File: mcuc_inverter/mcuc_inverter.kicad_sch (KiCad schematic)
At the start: 0 parts

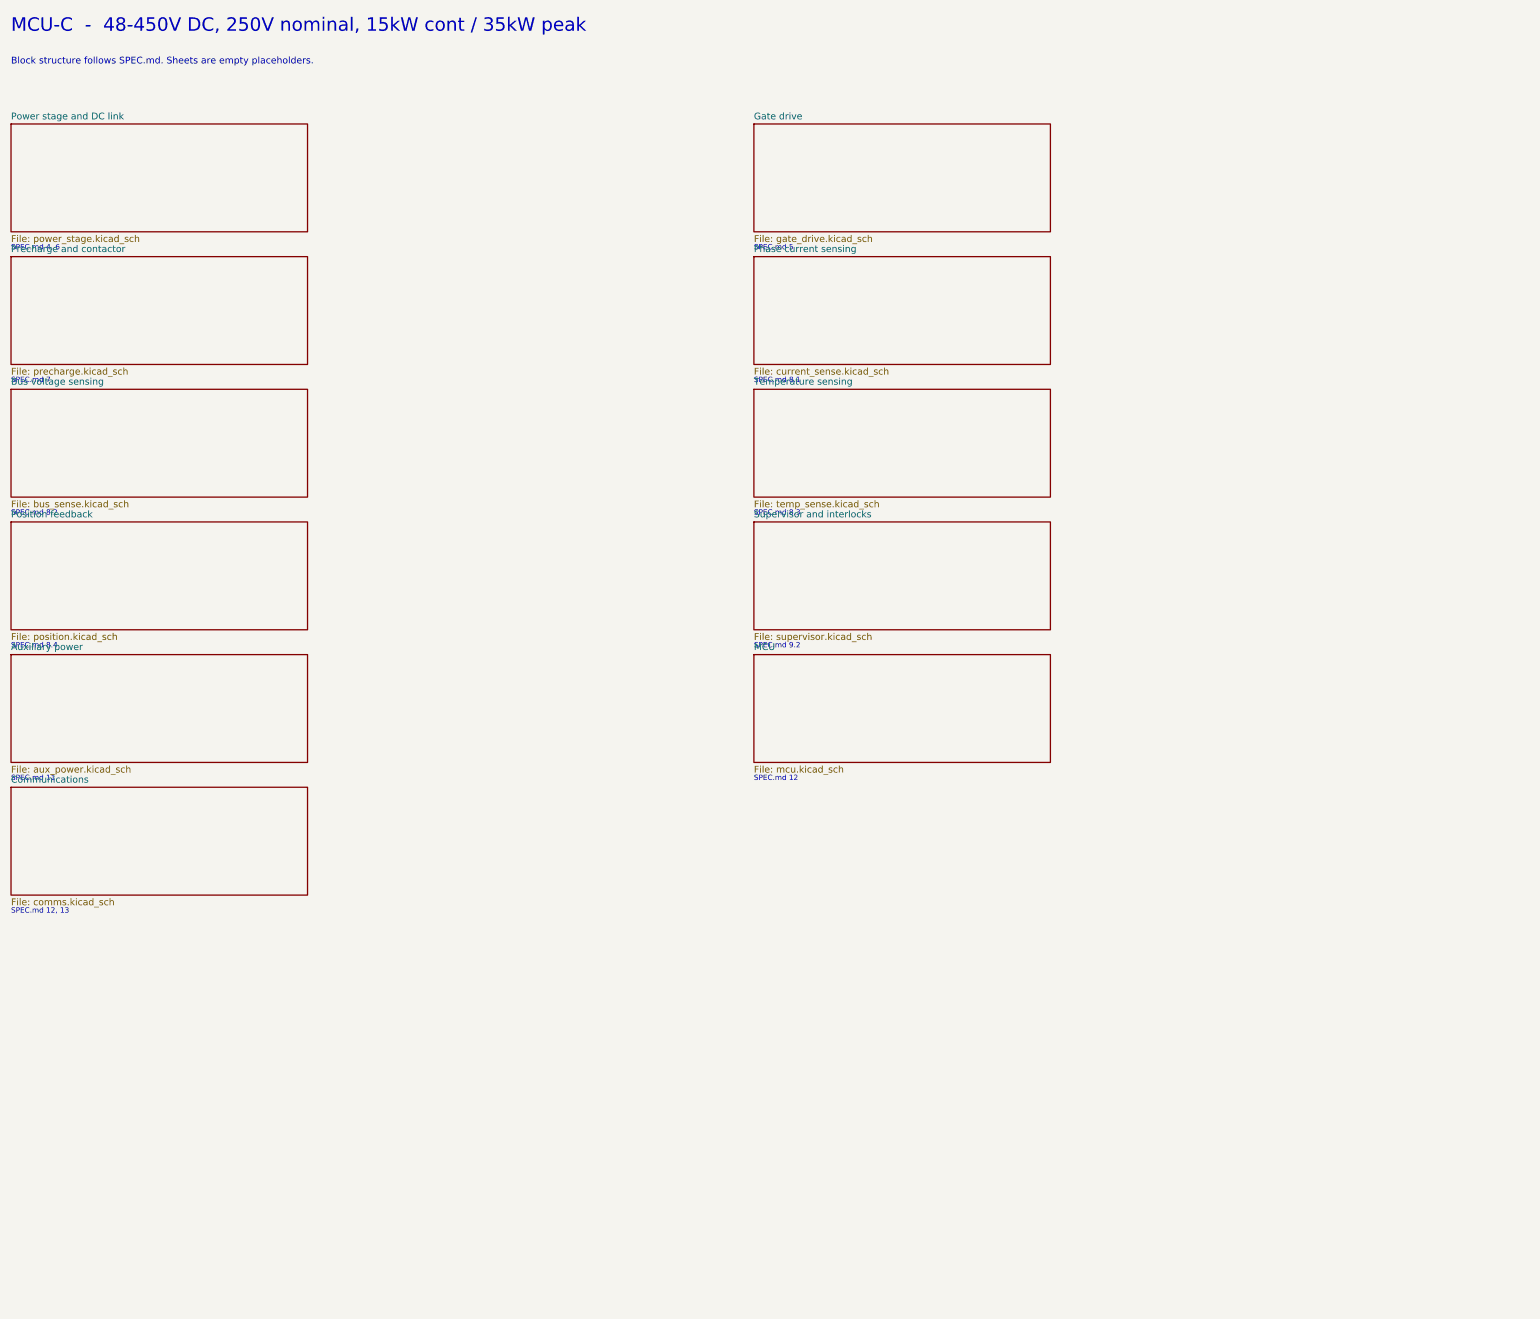
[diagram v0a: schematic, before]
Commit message: Design the supervisor interlock block
Adds docs/supervisor.md: the full logic design for the firmware-independent
hardware interlocks required by SPEC.md §9.2 -- overcurrent detect and latch,
fault aggregation, PWM overlap elimination and dead time. Includes the
24-signal interface, gate budget, and a failure-mode review done on the
assumption that firmware is hostile.

Two selections differ from the original PALTA board, both deliberate:

- Comparators run from +5 V, not 3.3 V. The LM2903's input common-mode
  ceiling is VCC-1.5V, so on 3.3 V it is 1.8 V -- below the 3.05 V positive
  trip point. The positive-overcurrent channel would never have asserted.
  Open-drain outputs still pull up to 3.3 V, so no level shifting is needed.
- 74HC replaces 74ACT. The dead-time RC assumes a CMOS threshold at
  0.5*VCC; 74ACT's TTL thresholds make the delay supply- and part-dependent.
  Predictable dead time beats ~10 ns of propagation delay here.

Adds tools/gen_skeleton.py, which generates the KiCad skeleton and records
the block interfaces, and ERC severities in mcuc_inverter.kicad_pro:
hier_label_mismatch stays an error, label_dangling and pin_not_connected
become warnings during build-out.

The interface is not emitted into the schematic yet (EMIT_INTERFACE=False).
Emitting it into empty sheets produces 96 legitimate dangling-label
violations, and copperhead check fails on warnings as well as errors, which
would leave the verification gate permanently red -- the same failure mode
that let the earlier generated documents through unchecked. The interface
lands in the same change as the components. Rationale in supervisor.md §9.

Verified: kicad-cli sch erc reports 0 violations and copperhead check is
green. With the interface temporarily emitted, ERC reported no
hier_label_mismatch, confirming all 24 names and directions agree across
every sheet boundary.

Co-Authored-By: Claude Opus 5 <noreply@anthropic.com>
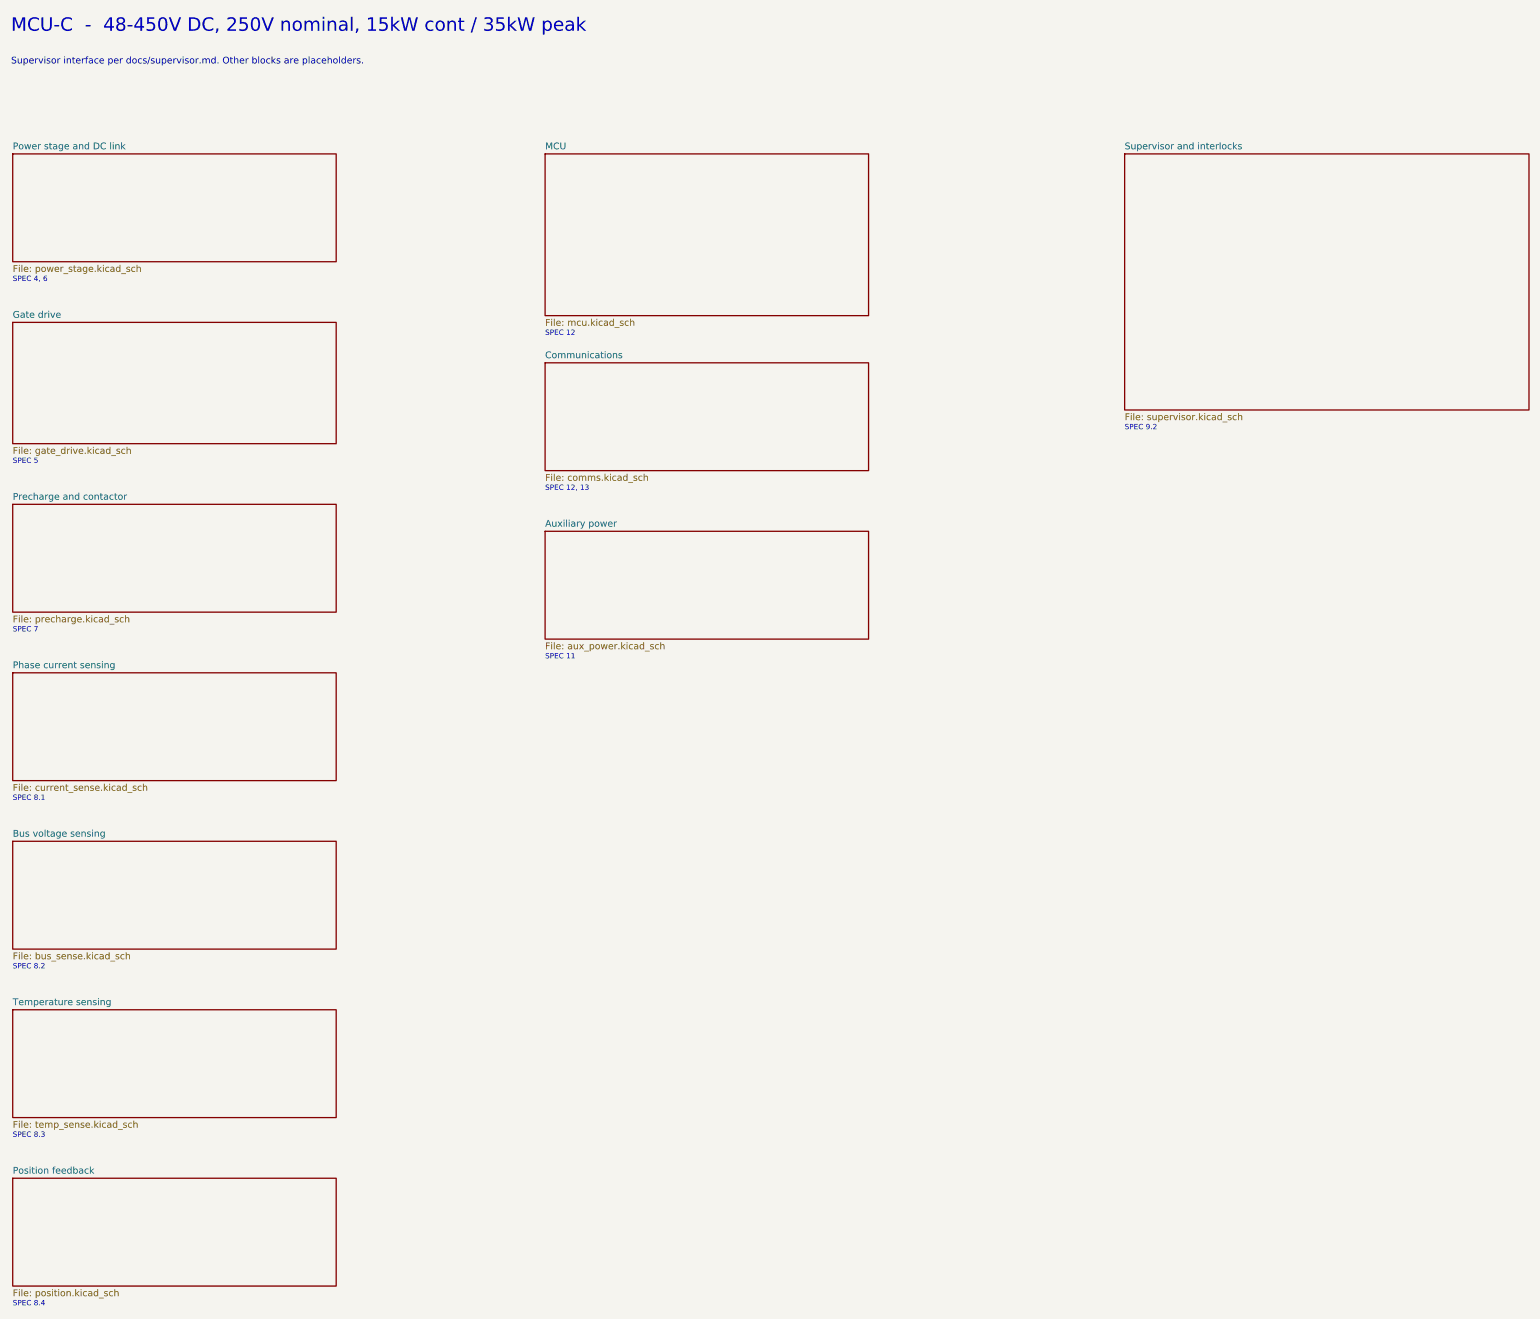
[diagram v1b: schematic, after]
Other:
- note added: "SPEC 11"
- note added: "SPEC 12"
- note added: "SPEC 12, 13"
- note added: "SPEC 4, 6"
- note added: "SPEC 5"
- note added: "SPEC 7"
- note added: "SPEC 8.1"
- note added: "SPEC 8.2"
- note added: "SPEC 8.3"
- note added: "SPEC 8.4"
- note added: "SPEC 9.2"
- note added: "Supervisor interface per docs/supervisor.md. Other blocks are placeholders."
- note removed: "Block structure follows SPEC.md. Sheets are empty placeholders."
- note removed: "SPEC.md 11"
- note removed: "SPEC.md 12"
- note removed: "SPEC.md 12, 13"
- note removed: "SPEC.md 4, 6"
- note removed: "SPEC.md 5"
- note removed: "SPEC.md 7"
- note removed: "SPEC.md 8.1"
- note removed: "SPEC.md 8.2"
- note removed: "SPEC.md 8.3"
- note removed: "SPEC.md 8.4"
- note removed: "SPEC.md 9.2"

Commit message: Place the supervisor overcurrent comparator front end
Implements docs/supervisor.md section 3 in the schematic: 13 components
across the threshold divider, six LM2903 comparator channels and the
wired-OR trip node.

A single three-resistor string (1k / 11k / 1k off +3V3) generates both
thresholds -- 3.046 V and 0.254 V, i.e. +/-280 A -- which keeps them
ratiometric with the rail the current sense is referenced to, so divider
tolerance and rail drift track out of the trip point.

Channel polarity: the positive trip puts V_TH_POS on IN+ and ISENSE on
IN-, the negative trip the other way round, so both pull the open-drain
output low on an overcurrent of either sign. All six outputs wire-OR onto
OC_TRIP_N with one 4.7k pull-up to +3V3 and a 100 pF filter.

Verified by netlist export rather than assumption:
  OC_TRIP_N  8 nodes  six comparator outputs + pull-up + filter
  V_TH_POS   6 nodes  divider tap, decoupling, three positive-channel IN+
  V_TH_NEG   6 nodes  divider tap, decoupling, three negative-channel IN-
  ISENSE_x   2 nodes  Ux.2 and Ux.5, the intended cross-pairing
  +5V        6 nodes  three LM2903 V+ and three decoupling caps
  GND       10 nodes
ERC reports 0 errors.

gen_skeleton.py now emits interface signals selectively via EMIT_SIGNALS
instead of all-or-nothing, so warnings stay proportional to what is built.
Six warnings remain -- 3 label_dangling and 3 pin_not_driven -- all saying
that current_sense does not exist yet so nothing drives ISENSE. Left in
place deliberately; they clear when that block is populated.

pin_not_driven joins the WIP warning severities. hier_label_mismatch stays
an error, since a boundary mismatch is a real defect at any build state.

Note that copperhead check fails on warnings as well as errors, so it reads
red while any block is unbuilt. kicad-cli sch erc --severity-error is the
meaningful gate during build-out and currently reports 0.

Co-Authored-By: Claude Opus 5 <noreply@anthropic.com>
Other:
- sheet Phase current sensing ports: added ISENSE_A, ISENSE_B, ISENSE_C; removed none
- sheet Supervisor and interlocks ports: added ISENSE_A, ISENSE_B, ISENSE_C; removed none
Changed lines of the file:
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@@
 		(instances
 			(project "mcuc_inverter"
-				(path "/bf2b1e33-8fc4-447a-8dc6-49e53bf48170"
+				(path "/c2a3c707-c5cb-4b38-83d3-7f8307d61589"
 					(page "2")
 				)
@@
 		(instances
 			(project "mcuc_inverter"
-				(path "/bf2b1e33-8fc4-447a-8dc6-49e53bf48170"
+				(path "/c2a3c707-c5cb-4b38-83d3-7f8307d61589"
 					(page "3")
 				)
@@
 		(instances
 			(project "mcuc_inverter"
-				(path "/bf2b1e33-8fc4-447a-8dc6-49e53bf48170"
+				(path "/c2a3c707-c5cb-4b38-83d3-7f8307d61589"
 					(page "4")
 				)
@@
 			)
 		)
-		(instances
-			(project "mcuc_inverter"
-				(path "/bf2b1e33-8fc4-447a-8dc6-49e53bf48170"
+		(pin "ISENSE_A" output
+			(at 81.28 140.97 0)
+			(effects
+				(font
+					(size 1.27 1.27)
+				)
+				(justify left)
+			)
+		)
+		(pin "ISENSE_B" output
+			(at 81.28 143.51000000000002 0)
+			(effects
+				(font
+					(size 1.27 1.27)
+				)
+				(justify left)
+			)
+		)
+		(pin "ISENSE_C" output
+			(at 81.28 146.05 0)
+			(effects
+				(font
+					(size 1.27 1.27)
+				)
+				(justify left)
+			)
+		)
+		(instances
+			(project "mcuc_inverter"
+				(path "/c2a3c707-c5cb-4b38-83d3-7f8307d61589"
 					(page "5")
 				)
@@
 		(instances
 			(project "mcuc_inverter"
-				(path "/bf2b1e33-8fc4-447a-8dc6-49e53bf48170"
+				(path "/c2a3c707-c5cb-4b38-83d3-7f8307d61589"
 					(page "6")
 				)
@@
 		(instances
 			(project "mcuc_inverter"
-				(path "/bf2b1e33-8fc4-447a-8dc6-49e53bf48170"
+				(path "/c2a3c707-c5cb-4b38-83d3-7f8307d61589"
 					(page "7")
 				)
@@
 		(instances
 			(project "mcuc_inverter"
-				(path "/bf2b1e33-8fc4-447a-8dc6-49e53bf48170"
+				(path "/c2a3c707-c5cb-4b38-83d3-7f8307d61589"
 					(page "8")
 				)
@@
 		(instances
 			(project "mcuc_inverter"
-				(path "/bf2b1e33-8fc4-447a-8dc6-49e53bf48170"
+				(path "/c2a3c707-c5cb-4b38-83d3-7f8307d61589"
 					(page "9")
 				)
@@
 		(instances
 			(project "mcuc_inverter"
-				(path "/bf2b1e33-8fc4-447a-8dc6-49e53bf48170"
+				(path "/c2a3c707-c5cb-4b38-83d3-7f8307d61589"
 					(page "10")
 				)
@@
 		(instances
 			(project "mcuc_inverter"
-				(path "/bf2b1e33-8fc4-447a-8dc6-49e53bf48170"
+				(path "/c2a3c707-c5cb-4b38-83d3-7f8307d61589"
 					(page "11")
 				)
@@
 			)
 		)
-		(instances
-			(project "mcuc_inverter"
-				(path "/bf2b1e33-8fc4-447a-8dc6-49e53bf48170"
+		(pin "ISENSE_A" input
+			(at 229.87 43.18 180)
+			(effects
+				(font
+					(size 1.27 1.27)
+				)
+				(justify right)
+			)
+		)
+		(pin "ISENSE_B" input
+			(at 229.87 45.72 180)
+			(effects
+				(font
+					(size 1.27 1.27)
+				)
+				(justify right)
+			)
+		)
+		(pin "ISENSE_C" input
+			(at 229.87 48.26 180)
+			(effects
+				(font
+					(size 1.27 1.27)
+				)
+				(justify right)
+			)
+		)
+		(instances
+			(project "mcuc_inverter"
+				(path "/c2a3c707-c5cb-4b38-83d3-7f8307d61589"
 					(page "12")
 				)
@@
 		)
 	)
+	(wire
+		(pts
+			(xy 81.28 140.97) (xy 86.36 140.97)
+		)
+		(stroke
+			(width 0)
+			(type default)
+		)
+	)
+	(label "ISENSE_A"
+		(at 86.36 140.97 0)
+		(fields_autoplaced yes)
+		(effects
+			(font
+				(size 1.27 1.27)
+			)
+			(justify left bottom)
+		)
+	)
+	(wire
+		(pts
+			(xy 81.28 143.51000000000002) (xy 86.36 143.51000000000002)
+		)
+		(stroke
+			(width 0)
+			(type default)
+		)
+	)
+	(label "ISENSE_B"
+		(at 86.36 143.51000000000002 0)
+		(fields_autoplaced yes)
+		(effects
+			(font
+				(size 1.27 1.27)
+			)
+			(justify left bottom)
+		)
+	)
+	(wire
+		(pts
+			(xy 81.28 146.05) (xy 86.36 146.05)
+		)
+		(stroke
+			(width 0)
+			(type default)
+		)
+	)
+	(label "ISENSE_C"
+		(at 86.36 146.05 0)
+		(fields_autoplaced yes)
+		(effects
+			(font
+				(size 1.27 1.27)
+			)
+			(justify left bottom)
+		)
+	)
+	(wire
+		(pts
+			(xy 229.87 43.18) (xy 224.79 43.18)
+		)
+		(stroke
+			(width 0)
+			(type default)
+		)
+	)
+	(label "ISENSE_A"
+		(at 224.79 43.18 180)
+		(fields_autoplaced yes)
+		(effects
+			(font
+				(size 1.27 1.27)
+			)
+			(justify right bottom)
+		)
+	)
+	(wire
+		(pts
+			(xy 229.87 45.72) (xy 224.79 45.72)
+		)
+		(stroke
+			(width 0)
+			(type default)
+		)
+	)
+	(label "ISENSE_B"
+		(at 224.79 45.72 180)
+		(fields_autoplaced yes)
+		(effects
+			(font
+				(size 1.27 1.27)
+			)
+			(justify right bottom)
+		)
+	)
+	(wire
+		(pts
+			(xy 229.87 48.26) (xy 224.79 48.26)
+		)
+		(stroke
+			(width 0)
+			(type default)
+		)
+	)
+	(label "ISENSE_C"
+		(at 224.79 48.26 180)
+		(fields_autoplaced yes)
+		(effects
+			(font
+				(size 1.27 1.27)
+			)
+			(justify right bottom)
+		)
+	)
